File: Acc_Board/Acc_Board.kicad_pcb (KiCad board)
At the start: 2 copper layers, 139.7 x 76.2 mm, 67 parts, among them J1 AIRs Power, J12 776087-1, J2 IsoSPI, J3 IMD BAT, J4 HV Power, J5 HVIL, J6 IMD, J7 Current Sensor, J8 Fans, J9 Shutdown IL, K1 Relay_SPST-NO, Q1 STS6NF20V, Q2 STS6NF20V, Q3 STS6NF20V, U1 ISO1050DUB, U10 DK1A1B-12V, U12 LTC6820, U15 MCP6004, U2 NUCLEO-L432KC, U3 DK1A1B-12V, U4 PQDE6W-Q110-S5-H-D, U5 R-78B5.0-2.0, U6 NSL-32, U7 DK1A1B-12V, U8 LM7809_TO220, U9 NSL-32

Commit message: minor acc board changes
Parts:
- removed D4: US1A, Diode_SMD:D_SMA
- removed U3: DK1A1B-12V, 1FS_2_Global_Footprint_Library:RELAY_DK2A_PAN
- added C13: C, Capacitor_SMD:C_0805_2012Metric_Pad1.18x1.45mm_HandSolder, F.Cu at (62.5, 102.4)
- added C15: C, Capacitor_SMD:C_0805_2012Metric_Pad1.18x1.45mm_HandSolder, F.Cu at (48.3, 25.4)
- added G***: LOGO, 1FS_2_Global_Footprint_Library:FORMULA SLUG, B.Cu at (80.3, 85.1)
- added J10: Conn_01x02_Pin, Connector_PinHeader_2.54mm:PinHeader_1x02_P2.54mm_Vertical, F.Cu at (57.7, 103.2)
- added R13: 3.9k, Resistor_SMD:R_0805_2012Metric_Pad1.20x1.40mm_HandSolder, F.Cu at (82.5, 102.9)
- added R19: 18k, Resistor_SMD:R_0805_2012Metric_Pad1.20x1.40mm_HandSolder, F.Cu at (86.4, 102.9)
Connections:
- net Net-(U2A-PA1) renamed /Buffered_C_Out
- net Net-(U2A-PA3) renamed /Buffered_C_Vref
- J12 pad 12: /Charge_Exit -> /Charge_Enable
- U10 pad 3: Net-(D4-A) -> Net-(U10-Pad3)
- U2 pad CN4_12: unconnected-(U2A-PA0-PadCN4_12) -> /GLV Voltage
- U2 pad CN4_5: unconnected-(U2A-PA2-PadCN4_5) -> /PA_2
- U7 pad 4: Net-(D4-K) -> Net-(U10-Pad3)
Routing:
- net /Charge_Enable: track 21.2 -> 109.7 mm, vias 1 -> 5
- net /Charge_Exit: track 88.6 -> 0.00 mm, vias 4 -> 0
- net Net-(U10-Pad3): track 0.00 -> 32.6 mm
- net Net-(D4-A): track 20.1 -> 0.00 mm
- net Net-(D4-K): track 12.5 -> 0.00 mm

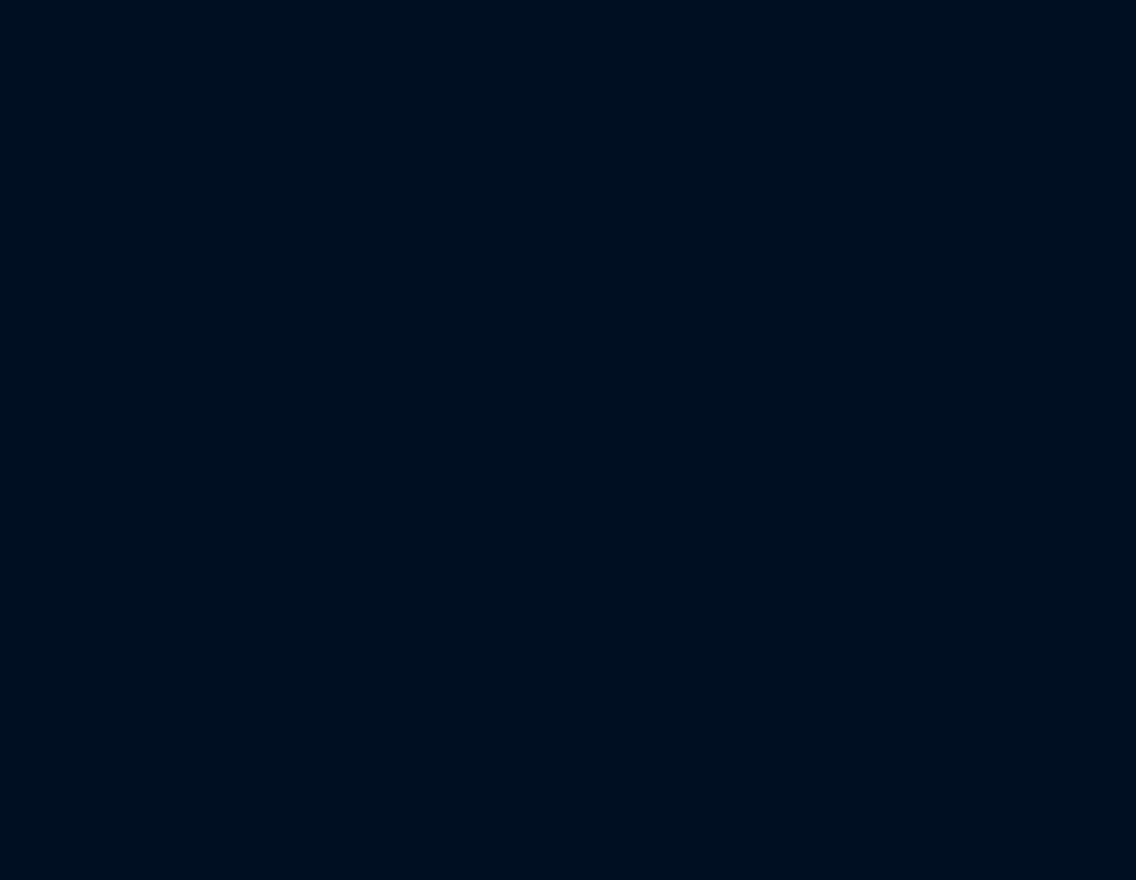
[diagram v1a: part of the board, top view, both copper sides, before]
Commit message: added latching logic to acc board schematic
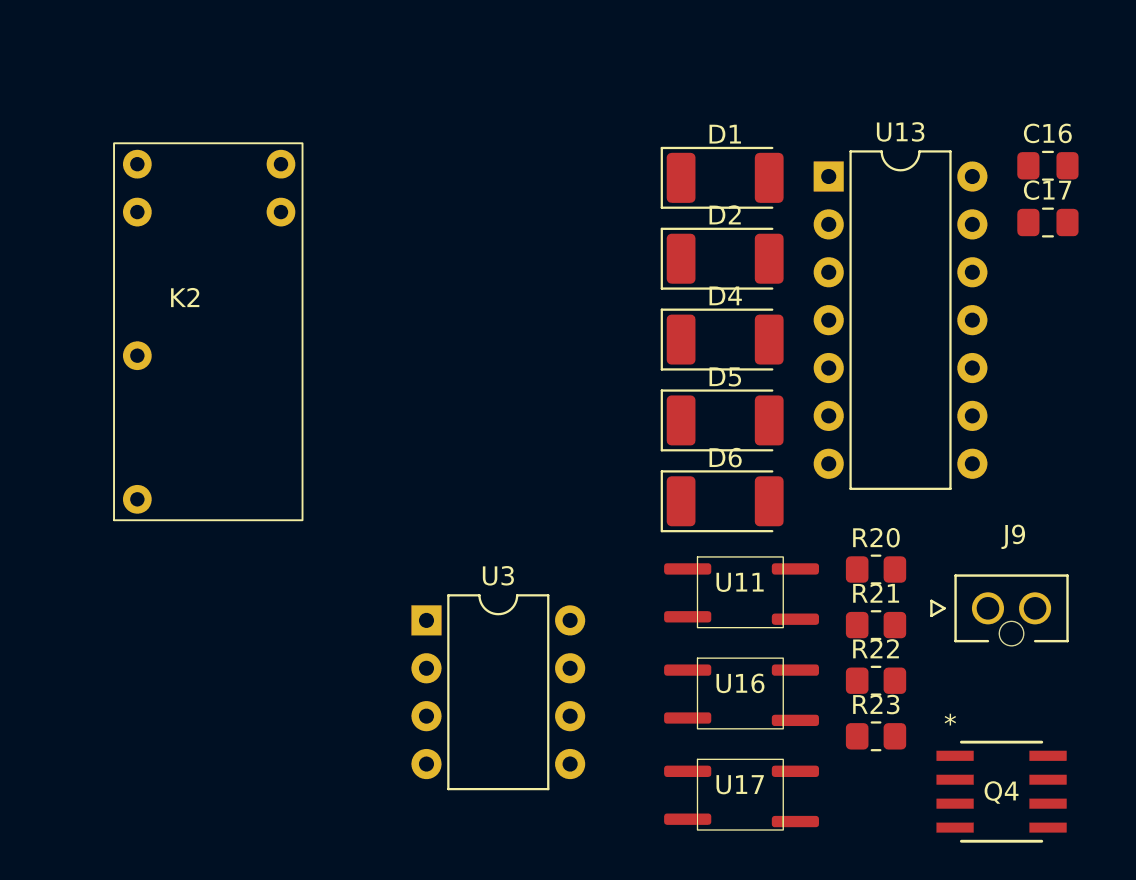
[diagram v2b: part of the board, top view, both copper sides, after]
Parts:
- added C16: 1uf, Capacitor_SMD:C_0805_2012Metric_Pad1.18x1.45mm_HandSolder, F.Cu at (149.8, 102.9)
- added C17: 100nf, Capacitor_SMD:C_0805_2012Metric_Pad1.18x1.45mm_HandSolder, F.Cu at (149.8, 105.9)
- added D1: D, Diode_SMD:D_2010_5025Metric_Pad1.52x2.65mm_HandSolder, F.Cu at (132.7, 103.5)
- added D2: D, Diode_SMD:D_2010_5025Metric_Pad1.52x2.65mm_HandSolder, F.Cu at (132.7, 107.8)
- added D4: D, Diode_SMD:D_2010_5025Metric_Pad1.52x2.65mm_HandSolder, F.Cu at (132.7, 112.1)
- added D5: D, Diode_SMD:D_2010_5025Metric_Pad1.52x2.65mm_HandSolder, F.Cu at (132.7, 116.4)
- added D6: D, Diode_SMD:D_2010_5025Metric_Pad1.52x2.65mm_HandSolder, F.Cu at (132.7, 120.7)
- added J9: Shutdown IL, 1FS_2_Global_Footprint_Library:MOLEX_1053091202, F.Cu at (146.6, 126.4)
- added K2: Latching Relay, 1FS_2_Global_Footprint_Library:Omron G6BK-1114P-US, F.Cu at (104.0, 110.4)
- added Q4: STS6NF20V, 1FS_2_Global_Footprint_Library:SO-8_STM, F.Cu at (147.3, 136.1)
- added R20: 2.4M, Resistor_SMD:R_0805_2012Metric_Pad1.20x1.40mm_HandSolder, F.Cu at (140.7, 124.3)
- added R21: 374, Resistor_SMD:R_0805_2012Metric_Pad1.20x1.40mm_HandSolder, F.Cu at (140.7, 127.2)
- added R22: 665, Resistor_SMD:R_0805_2012Metric_Pad1.20x1.40mm_HandSolder, F.Cu at (140.7, 130.2)
- added R23: 205, Resistor_SMD:R_0805_2012Metric_Pad1.20x1.40mm_HandSolder, F.Cu at (140.7, 133.2)
- added U11: NSL-32, 1FS_2_Global_Footprint_Library:OptoCoupler 6-SOP, F.Cu at (133.5, 125.5)
- added U13: NAND, Package_DIP:DIP-14_W7.62mm, F.Cu at (138.2, 103.5)
- added U16: NSL-32, 1FS_2_Global_Footprint_Library:OptoCoupler 6-SOP, F.Cu at (133.5, 130.9)
- added U17: NSL-32, 1FS_2_Global_Footprint_Library:OptoCoupler 6-SOP, F.Cu at (133.5, 136.2)
- added U3: LM555N, Package_DIP:DIP-8_W7.62mm, F.Cu at (116.8, 127.0)
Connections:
- U10 pad 4: Net-(J9-Pad1) -> Net-(J9-Pad2)
- U6 pad 1: /BMS_FAULT -> /BMS_FAULT_5V
- U9 pad 1: /IMD_FAULT -> /IMD_FAULT_5V

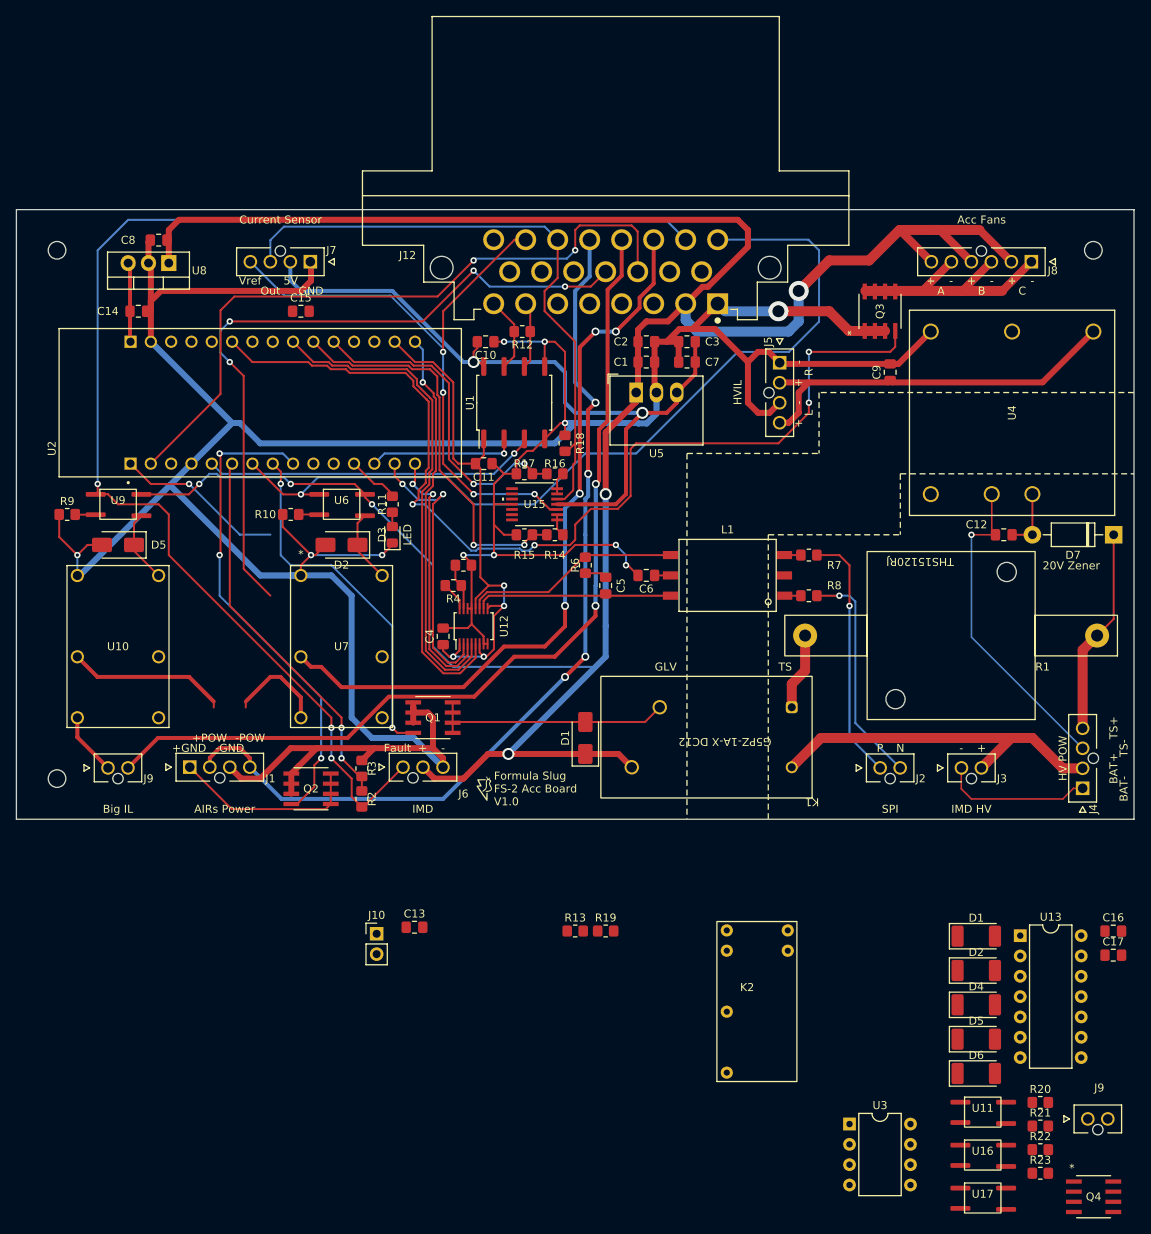
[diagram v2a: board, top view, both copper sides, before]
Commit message: components placed on acc board; traces in progress
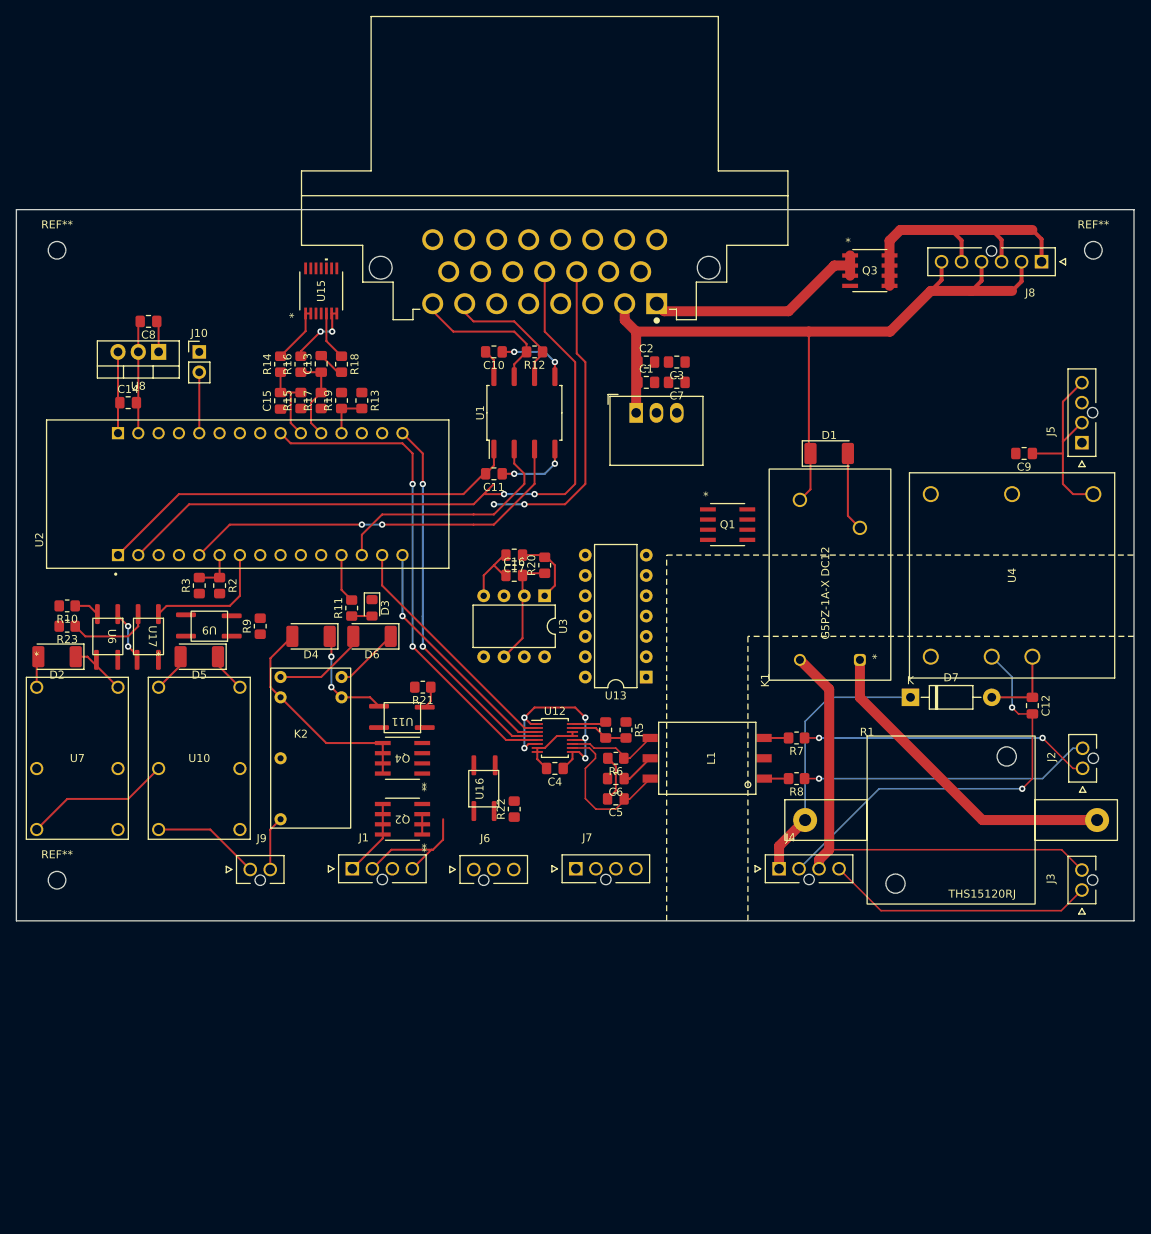
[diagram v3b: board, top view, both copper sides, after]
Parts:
- removed the D1 at (132.7, 103.5)
- removed the D1 at (83.8, 78.7)
- removed the D2 at (132.7, 107.8)
- removed the D2 at (53.3, 54.6)
- removed the D5 at (132.7, 116.4)
- removed the D5 at (25.4, 54.6)
- removed G*** (x2): LOGO, 1FS_2_Global_Footprint_Library:FORMULA SLUG
- removed the J9 at (146.6, 126.4)
- removed the J9 at (24.1, 82.5)
- added D1: D, Diode_SMD:D_2010_5025Metric_Pad1.52x2.65mm_HandSolder, F.Cu at (114.3, 43.2)
- added D2: D, Diode_SMD:D_2010_5025Metric_Pad1.52x2.65mm_HandSolder, F.Cu at (17.8, 68.6)
- added D5: D, Diode_SMD:D_2010_5025Metric_Pad1.52x2.65mm_HandSolder, F.Cu at (35.6, 68.6)
- added J9: Shutdown IL, 1FS_2_Global_Footprint_Library:MOLEX_1053091202, F.Cu at (41.9, 95.2)
- R21: value 374 -> 370
- moved R23 139.5 mm to (19.1, 64.8), turned to 180 degrees
- moved U17 125.7 mm to (29.2, 66.0), turned to -90 degrees
- moved Q4 102.3 mm to (61.0, 81.3), turned to 180 degrees
- moved D4 95.1 mm to (49.5, 66.0), turned to 180 degrees
- moved R21 94.7 mm to (63.5, 72.4), turned to 180 degrees
- moved D6 93.2 mm to (57.1, 66.0), turned to 180 degrees
- moved R20 91.4 mm to (78.7, 57.1), turned to 90 degrees
- moved C17 90.0 mm to (74.9, 55.9), turned to 180 degrees
- moved U11 87.7 mm to (61.0, 76.2), turned to 180 degrees
- moved C16 87.1 mm to (74.9, 58.4)
- moved J7 82.8 mm to (82.6, 95.1), turned to 0 degrees
- moved R22 78.3 mm to (74.9, 87.6), turned to 90 degrees
- moved U16 77.4 mm to (71.1, 85.1), turned to 90 degrees
- moved U3 76.2 mm to (78.7, 61.0), turned to -90 degrees
- moved J10 76.0 mm to (35.6, 30.5)
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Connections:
- J12 pad 16: /BMS_FAULT -> /BMS_FAULT_5V
- J12 pad 17: /IMD_FAULT -> /IMD_FAULT_5V
- J12 pad 23: unconnected-(J12-Pad23) -> /SH_RESET
- J4 pad 1: /BAT- -> /TS+
- J4 pad 2: /BAT+ -> /TS-
- J4 pad 3: /TS- -> /BAT+
- J4 pad 4: /TS+ -> /BAT-
- R22 pad 2: unconnected-(R22-Pad2) -> GND
- R23 pad 2: unconnected-(R23-Pad2) -> GND
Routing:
- net GND: track 465.7 -> 104.6 mm, vias 11 -> 4
- net +12V: track 326.9 -> 101.4 mm, vias 6 -> 0
- net /IMD_FAULT: track 170.7 -> 0.00 mm, vias 3 -> 0
- net /Fan_Control: track 126.3 -> 0.00 mm, vias 4 -> 0
- net /Shutdown_ACC_OUT: track 114.7 -> 0.00 mm, vias 2 -> 0
- net /AIRS+_12V: track 113.8 -> 16.3 mm, vias 4 -> 0
- net /BMS_FAULT: track 108.6 -> 16.2 mm, vias 1 -> 0
- net /Shutdown_ACC_IN: track 92.2 -> 0.00 mm, vias 4 -> 0
- net +5V: track 93.2 -> 11.9 mm, vias 2 -> 0
- net /Current_Vref: track 78.7 -> 0.00 mm, vias 4 -> 0
- net /Current_Output: track 77.8 -> 6.12 mm
- net /Precharge_Control: track 60.9 -> 0.00 mm, vias 3 -> 0
- net /Precharge_Relay: track 45.1 -> 0.00 mm, vias 2 -> 0
- net /IMD_Status: track 48.0 -> 5.35 mm, vias 2 -> 0
- net /Buffered_C_Vref: track 50.1 -> 10.7 mm, vias 2 -> 0
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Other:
- board size 139.7 x 76.2 mm -> 139.7 x 88.9 mm
- board text removed: "+"
- board text removed: "+GND"
- board text removed: "+POW"
- board text removed: "-"
- board text removed: "-GND"
- board text removed: "-POW"
- board text removed: "20V Zener"
- board text removed: "5V"
- board text removed: "A"
- board text removed: "AIRs Power"
- board text removed: "Acc Fans"
- board text removed: "B"
- board text removed: "BAT+"
- board text removed: "BAT-"
- board text removed: "Big IL"
- board text removed: "C"
- board text removed: "Current Sensor"
- board text removed: "Fault"
- board text removed: "Formula Slug FS-2 Acc Board V1.0"
- board text removed: "GLV"
- board text removed: "GND"
- board text removed: "HV POW"
- board text removed: "HVIL"
- board text removed: "IMD"
- board text removed: "IMD HV"
- board text removed: "L"
- board text removed: "LED"
- board text removed: "N"
- board text removed: "Out"
- board text removed: "P"
- board text removed: "R"
- board text removed: "SPI"
- board text removed: "TS"
- board text removed: "TS+"
- board text removed: "TS-"
- board text removed: "Vref"

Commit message: acc board: all traces done; ground plane made
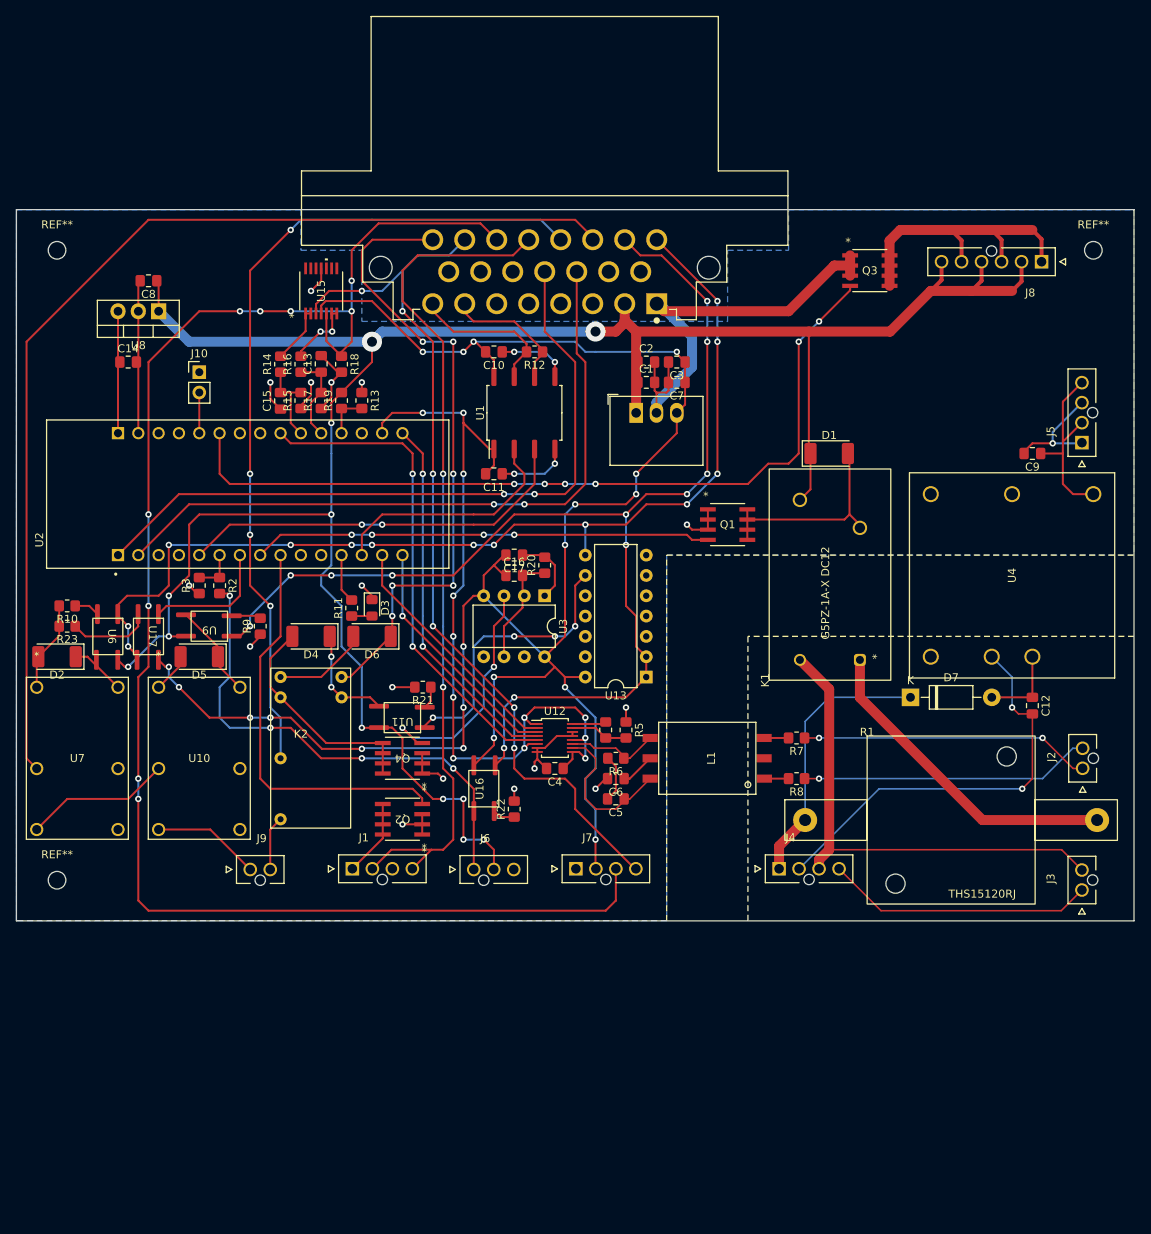
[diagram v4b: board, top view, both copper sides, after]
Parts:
- moved C8 5.08 mm to (29.2, 21.6)
- moved U8 5.08 mm to (30.5, 25.4)
- moved C14 5.08 mm to (26.7, 31.8)
- moved J10 2.54 mm to (35.6, 33.0)
- moved C9 1.04 mm to (139.7, 43.2)
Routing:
- net +5V: track 11.9 -> 240.9 mm, vias 0 -> 20
- net /Current_Output: track 6.12 -> 200.8 mm, vias 0 -> 9
- net +12V: track 101.4 -> 289.9 mm, vias 0 -> 12
- net /IMD_FAULT_5V: track 0.00 -> 152.1 mm, vias 0 -> 12
- net /Shutdown_ACC_IN: track 0.00 -> 132.2 mm
- net /BMS_FAULT_5V: track 5.95 -> 128.0 mm, vias 2 -> 13
- net /Current_Vref: track 0.00 -> 113.0 mm, vias 0 -> 6
- net /Shutdown_ACC_OUT: track 0.00 -> 105.0 mm, vias 0 -> 4
- net /Fan_Control: track 0.00 -> 103.2 mm, vias 0 -> 6
- net GND: track 104.6 -> 207.5 mm, vias 4 -> 21
- net /AIRS+_12V: track 16.3 -> 106.1 mm, vias 0 -> 2
- net /SH_RESET: track 8.25 -> 80.6 mm, vias 0 -> 6
- net +3.3V: track 31.0 -> 101.3 mm, vias 5 -> 12
- net /IMD_FAULT: track 0.00 -> 62.7 mm, vias 0 -> 4
- net /Precharge_Relay: track 0.00 -> 57.3 mm, vias 0 -> 4
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- added copper zone on B.Cu, net GND
